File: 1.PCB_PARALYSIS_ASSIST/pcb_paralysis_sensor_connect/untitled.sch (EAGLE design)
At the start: 9 parts

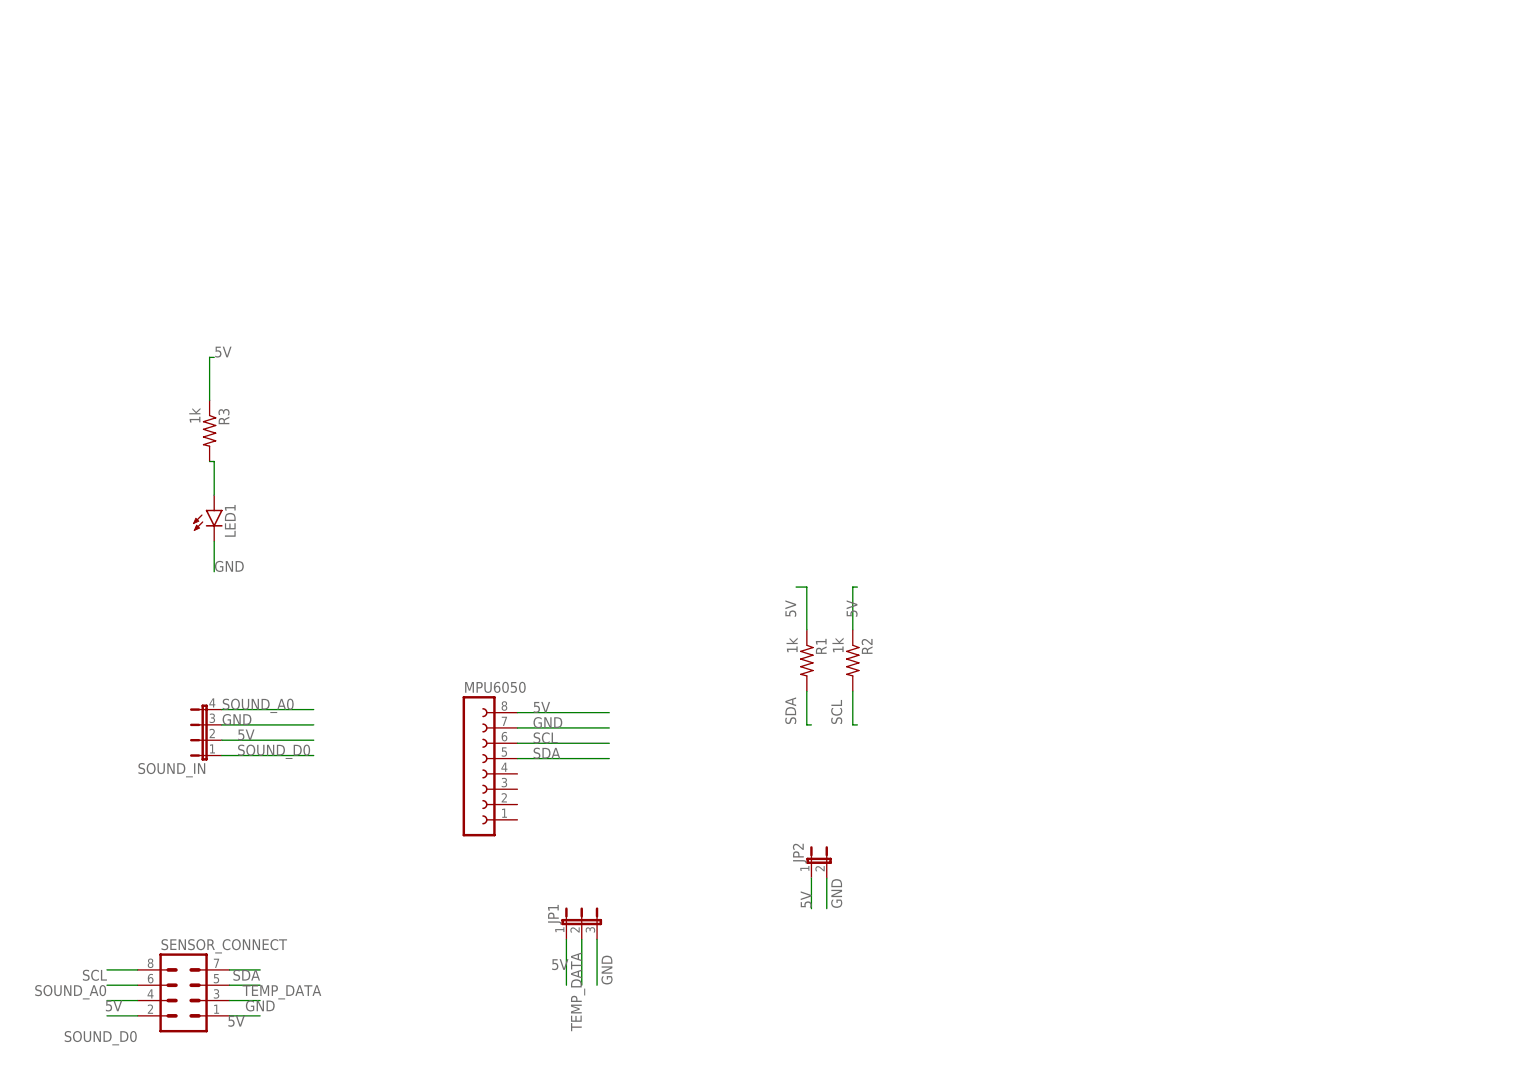
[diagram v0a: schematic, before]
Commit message: updated version_2 layout
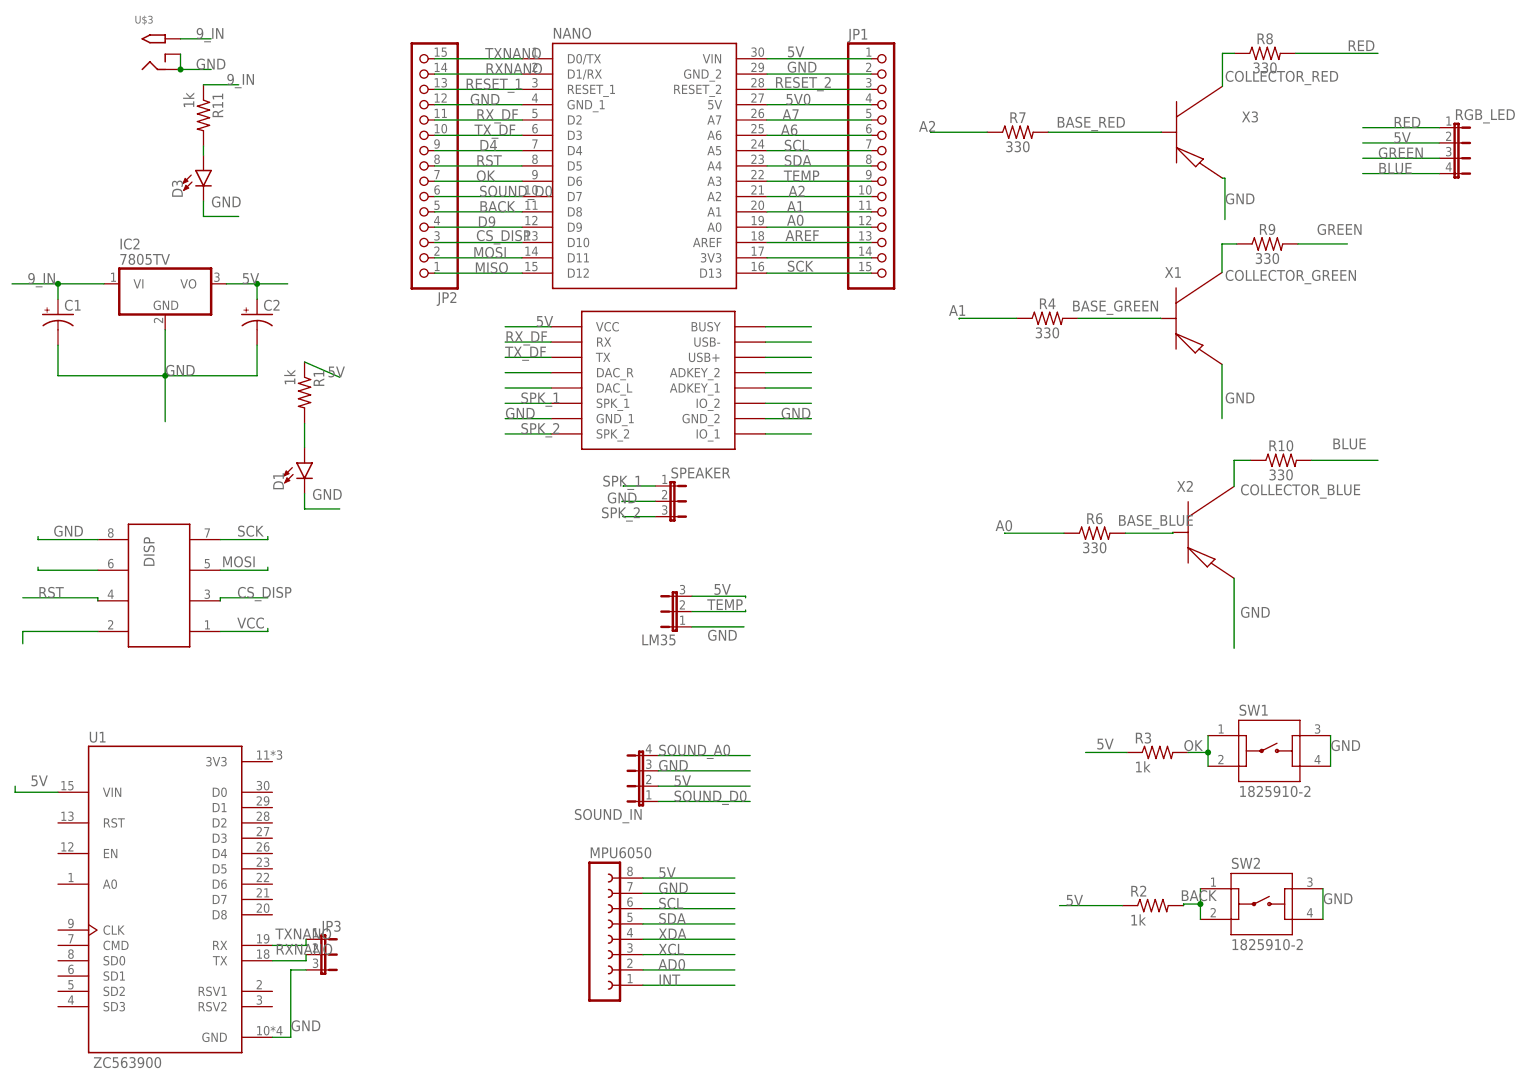
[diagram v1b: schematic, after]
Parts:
- removed LED1: (no value), led:LEDCHIP-LED0805
- removed SENSOR_CONNECT: (no value), con-lstb:MA04-2
- added C1, C2: (no value), adafruit:CPOL-USE3.5-8
- added D1, D3: (no value), SparkFun-LED:LED3MM
- added DISP: (no value), Wurth_Elektronik_Electromechanic_Wire_to_Board_Connectors_rev19a:612008235121
- added IC2: 7805TV, linear:7805TV
- added JP3: (no value), jumper:JP2W
- added LM35, SPEAKER: (no value), jumper:JP2E
- added NANO: A000005, A000005:A000005
- added R10, R4, R6, R7, R8, R9: 330, SparkFun-Resistors:330OHM-HORIZ-1/10W-5%
- added R11: 1k, adafruit:R-US_M0805
- added RGB_LED: (no value), jumper:JP4E
- added SW1, SW2: 1825910-2, 1825910-2:1825910-2
- added U$1: DFPLAYER, DFPlayer_v1:DFPLAYER
- added U$3: 2.1MMJACKTHM, adafruit:2.1MMJACKTHM
- added U1: ZC563900, nodemcuZC563900:ZC563900
- added X1, X2, X3: (no value), sym:2N3906
- JP1: device jumper:JP2W -> adafruit:PINHD-1X15
- JP2: device jumper:JP1E -> adafruit:PINHD-1X15
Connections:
- removed net TEMP_DATA: JP1.2, SENSOR_CONNECT.5
- new net 5V0: JP1.4, NANO.5V
- new net 9_IN: C1.+, IC2.VI, R11.1, U$3.TIP
- new net A0: JP1.12, NANO.A0, R6.1
- new net A1: JP1.11, NANO.A1, R4.1
- new net A2: JP1.10, NANO.A2, R7.1
- new net A6: JP1.6, NANO.A6
- new net A7: JP1.5, NANO.A7
- new net AD0: MPU6050.2
- new net AREF: JP1.13, NANO.AREF
- new net BACK: JP2.5, NANO.D8, R2.2, SW2.1, SW2.2
- new net BASE_BLUE: R6.2, X2.B
- new net BASE_GREEN: R4.2, X1.B
- new net BASE_RED: R7.2, X3.B
- new net BLUE: R10.2, RGB_LED.4
- new net COLLECTOR_BLUE: R10.1, X2.C
- new net COLLECTOR_GREEN: R9.1, X1.C
- new net COLLECTOR_RED: R8.1, X3.C
- new net CS_DISP: DISP.3, JP2.3, NANO.D10
- new net D4: JP2.9, NANO.D4
- new net D9: JP2.4, NANO.D9
- new net GREEN: R9.2, RGB_LED.3
- new net INT: MPU6050.1
- new net MISO: JP2.1, NANO.D12
- new net MOSI: DISP.5, JP2.2, NANO.D11
- new net N$13: U$1.DAC_R
- new net N$14: U$1.DAC_L
- new net N$18: U$1.BUSY
- new net N$19: U$1.USB-
- new net N$2: D3.A, R11.2
- new net N$20: U$1.USB+
- new net N$21: U$1.ADKEY_2
- new net N$22: U$1.ADKEY_1
- new net N$23: U$1.IO_2
- new net N$25: U$1.IO_1
- new net N$3: D1.A, R1.2
- new net N$5: DISP.6
- new net N$8: JP1.14, NANO.3V3
- new net OK: JP2.7, NANO.D6, R3.2, SW1.1, SW1.2
- new net RED: R8.2, RGB_LED.1
- new net RESET_1: JP2.13, NANO.RESET_1
- new net RESET_2: JP1.3, NANO.RESET_2
- new net RST: DISP.4, JP2.8, NANO.D5
- new net RXNANO: JP2.14, JP3.2, NANO.D1/RX, U1.TX
- new net RX_DF: JP2.11, NANO.D2, U$1.RX
- new net SCK: DISP.7, JP1.15, NANO.D13
- new net SPK_1: SPEAKER.1, U$1.SPK_1
- new net SPK_2: SPEAKER.3, U$1.SPK_2
- new net TEMP: JP1.9, LM35.2, NANO.A3
- new net TXNANO: JP2.15, JP3.1, NANO.D0/TX, U1.RX
- new net TX_DF: JP2.10, NANO.D3, U$1.TX
- new net VCC: DISP.1
- new net XCL: MPU6050.3
- new net XDA: MPU6050.4
- net 5V: now also C2.+, IC2.VO, LM35.3, NANO.VIN, RGB_LED.2, U$1.VCC, U1.VIN; no longer JP2.1, SENSOR_CONNECT.1, SENSOR_CONNECT.4
- net GND: now also C1.-, C2.-, D1.C, D3.C, DISP.8, IC2.GND, JP1.2, JP2.12, JP3.3, LM35.1, NANO.GND_1, NANO.GND_2, SPEAKER.2, SW1.3, SW1.4, SW2.3, SW2.4, U$1.GND_1, U$1.GND_2, U$3.RING, U$3.RING_SW, U1.GND, X1.E, X2.E, X3.E; no longer JP1.3, JP2.2, LED1.C, SENSOR_CONNECT.3
- net N$1: now also DISP.2; no longer LED1.A, R3.2
- net SCL: now also JP1.7, NANO.A5; no longer R2.2, SENSOR_CONNECT.8
- net SDA: now also JP1.8, NANO.A4; no longer R1.2, SENSOR_CONNECT.7
- net SOUND_A0: no longer SENSOR_CONNECT.6
- net SOUND_D0: now also JP2.6, NANO.D7; no longer SENSOR_CONNECT.2
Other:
- moved on the sheet: MPU6050, R1, R2, R3, SOUND_IN
